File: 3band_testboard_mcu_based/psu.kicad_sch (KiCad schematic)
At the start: 17 parts, among them J5 Battery in, U2 AMS1117-3.3, U3 AMS1117-3.3, U6 AMS1117-3.3

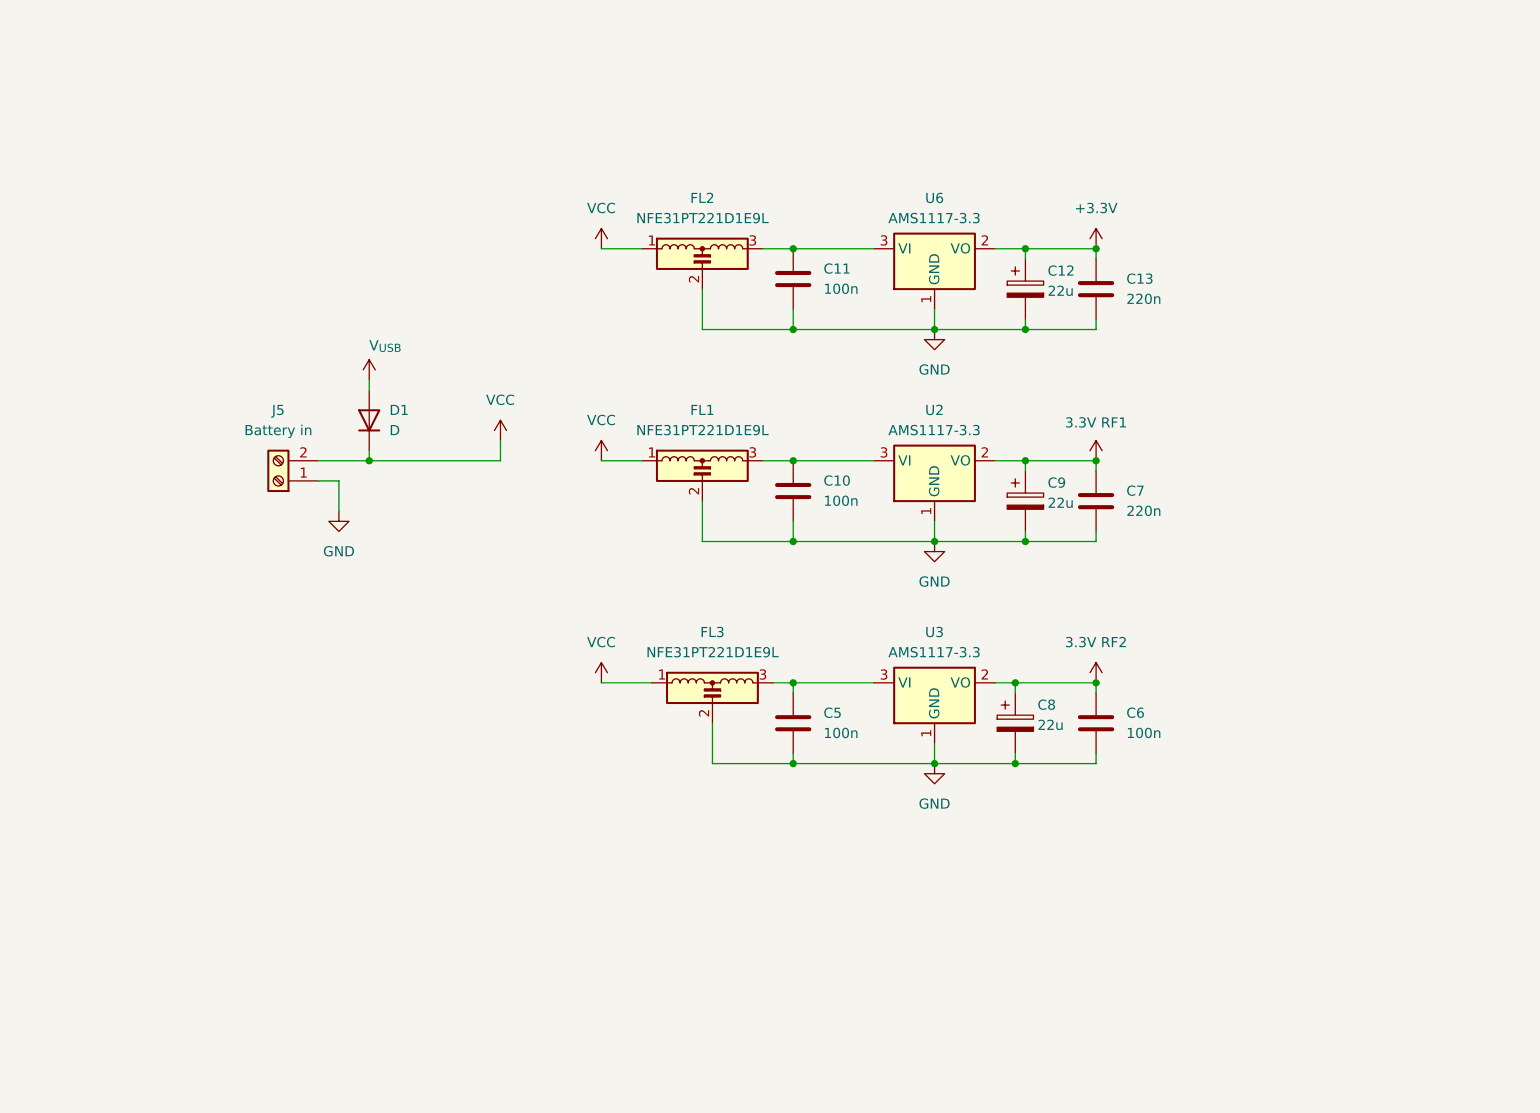
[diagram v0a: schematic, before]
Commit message: Færdiggjorde GPIO
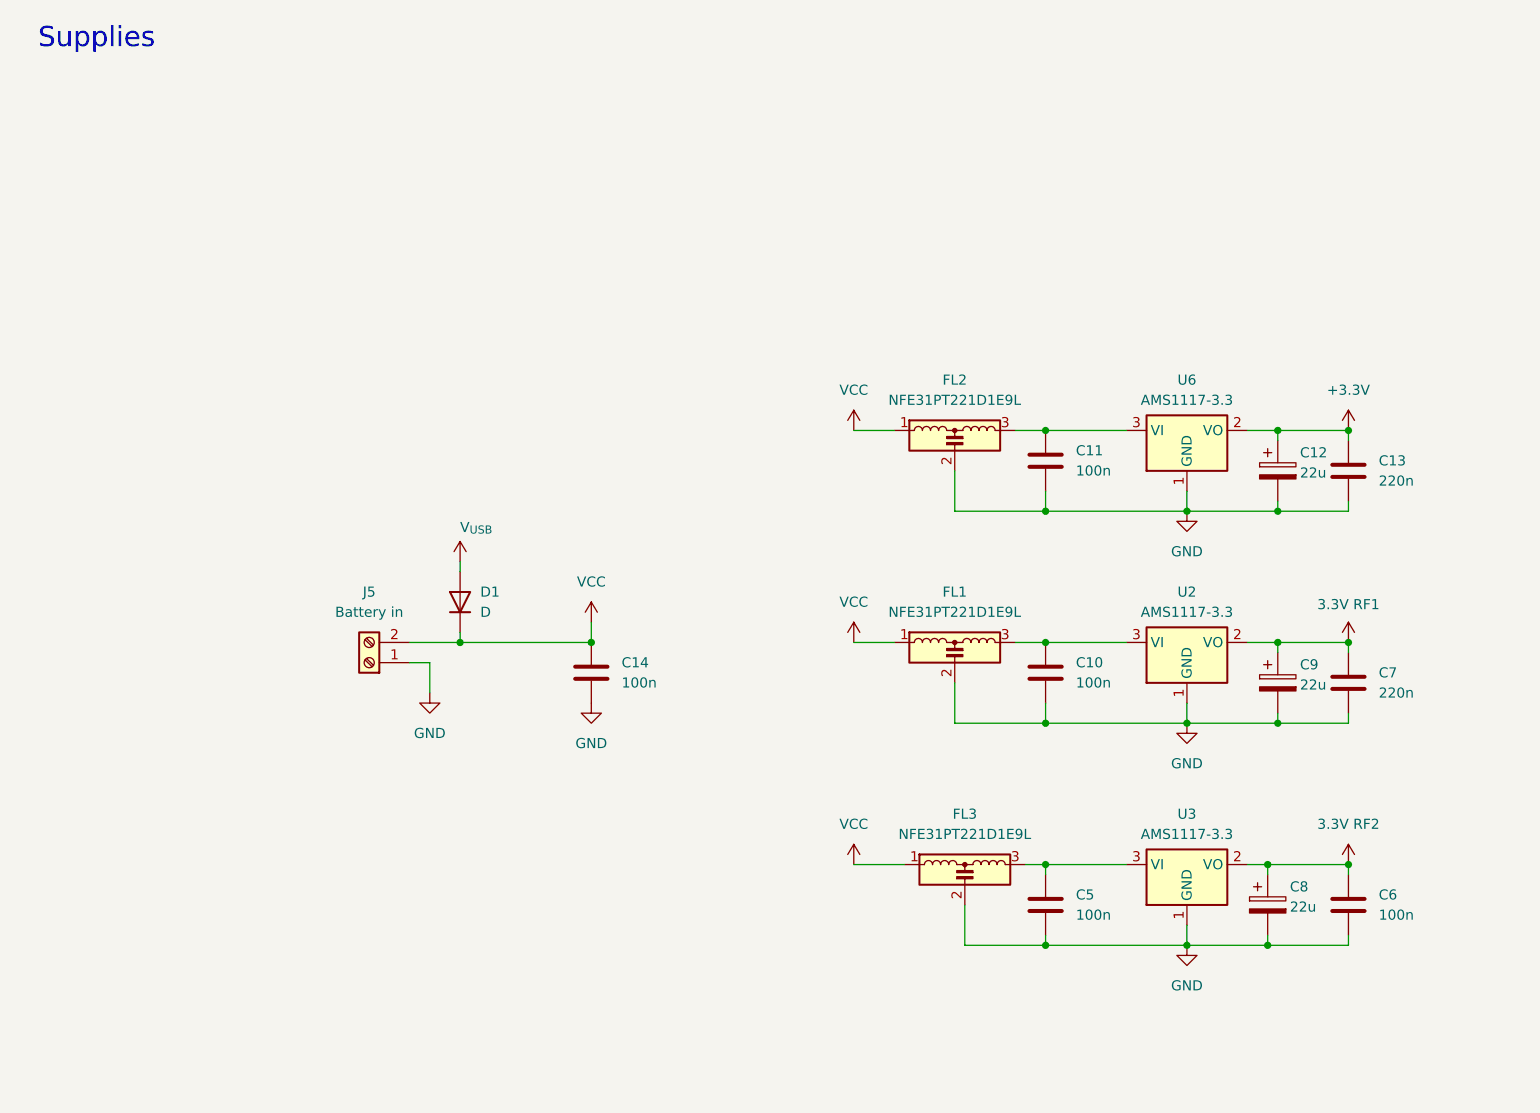
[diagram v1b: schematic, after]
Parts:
- added C14: 100n, Capacitor_SMD:C_0603_1608Metric, symbol Device:C
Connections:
- net GND: now also C14.2
- net VCC: now also C14.1
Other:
- note added: "Supplies"
- company: (none) -> AAU-connectivity
- title: (none) -> 3-band-LoRa testboard
- moved on the sheet: C10, C11, C12, C13, C5, C6, C7, C8, C9, D1, FL1, FL2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

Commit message: DRC check, and price
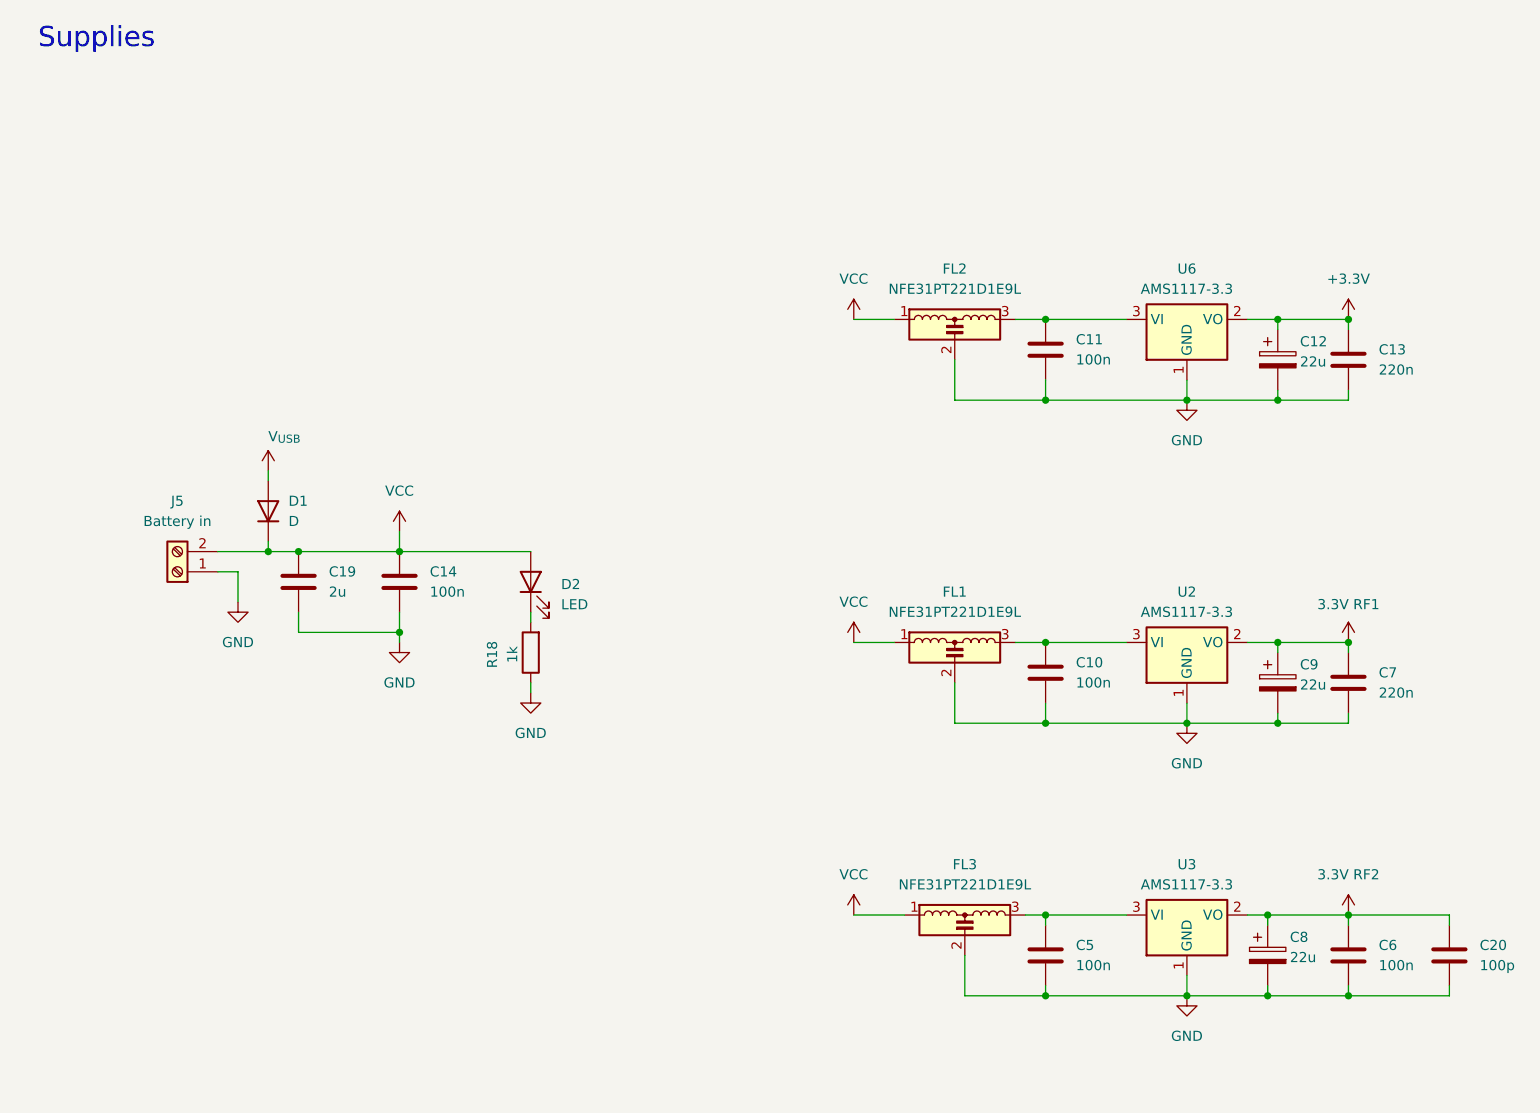
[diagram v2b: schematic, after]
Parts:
- added C19: 2u, Capacitor_SMD:C_1206_3216Metric_Pad1.33x1.80mm_HandSolder, symbol Device:C
- added C20: 100p, Capacitor_SMD:C_0603_1608Metric, symbol Device:C
- added D2: LED, LED_THT:LED_D3.0mm, symbol Device:LED
- added R18: 1k, Resistor_SMD:R_0603_1608Metric_Pad0.98x0.95mm_HandSolder, symbol Device:R
- C12, C8, C9: footprint Capacitor_SMD:C_1206_3216Metric -> Capacitor_THT:CP_Radial_D5.0mm_P2.50mm
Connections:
- net 3.3V RF2: now also C20.1
- net GND: now also C19.2, C20.2, R18.1
- net VCC: now also C19.1, D2.2 (A)
- new net: D2.1 (K), R18.2
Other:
- moved on the sheet: C11, C12, C13, C14, C5, C6, C8, D1, FL2, FL3, J5, U3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

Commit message: Prisoverslag
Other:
- note added: "Supply for ESP32 & IO"
- note added: "Supply for LBAA0XV2GT-001"
- note added: "Supply for rfm96w"
- moved on the sheet: C14, C19, C20, C5, C6, C8, D1, D2, FL3, J5, R18, U3
